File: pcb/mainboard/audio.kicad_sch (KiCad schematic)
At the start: 28 parts, among them J400 AudioJack3_SwitchT, U400 CS43130, U401 ADP150-1.8, U402 ADP150-1.8, Y400 22.5792MHz

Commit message: Mainboard schematics WIP
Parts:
- removed C400: 10uF, Capacitor_SMD:C_0402_1005Metric, symbol Device:C
- removed C416: 2.2uF, Capacitor_SMD:C_0402_1005Metric, symbol Device:C
- removed C417, C418: 1uF, Capacitor_SMD:C_0402_1005Metric, symbol Device:C
- removed J400: AudioJack3_SwitchT, footprint:PJ-327E, symbol symbols:AudioJack3_SwitchT
- removed R400: 33, Resistor_SMD:R_0402_1005Metric, symbol Device:R
- removed U400: CS43130, Package_DFN_QFN:QFN-40-1EP_5x5mm_P0.4mm_EP3.6x3.6mm_ThermalVias, symbol symbols:CS43130
- removed U401, U402: ADP150-1.8, footprint:CSP-4_2x2_0.8x0.8mm, symbol symbols:ADP150-1.8
- removed Y400: 22.5792MHz, Oscillator:Oscillator_SMD_Abracon_ASE-4Pin_3.2x2.5mm, symbol Device:Crystal_GND24
- added J401: AudioJack3, footprint:PJ-208, symbol Connector:AudioJack3
- added L401, L402: 120R, Inductor_SMD:L_0603_1608Metric, symbol Device:L
- added L403, L404: 15uH, Inductor_SMD:L_0603_1608Metric, symbol Device:L
- added LS401: Speaker, Buzzer_Beeper:Buzzer_D14mm_H7mm_P10mm, symbol Device:Speaker
- added R403, R404, R405: 22R, Resistor_SMD:R_0402_1005Metric, symbol Device:R
- added U402: FSA2269UMX, Package_DFN_QFN:UQFN-10_1.4x1.8mm_P0.4mm, symbol symbols:FSA2269UMX
- added U403: WM8978, Package_DFN_QFN:QFN-32-1EP_5x5mm_P0.5mm_EP3.45x3.45mm_ThermalVias, symbol symbols:WM8978
- C401, C402: value 100nF -> 220nF; LCSC (none) -> C880414; Ref.Price (none) -> 0.0036
- C403, C404: value 18pF -> 220nF; LCSC (none) -> C880414; Ref.Price (none) -> 0.0036
- C405: value 100nF -> 10uF/6.3V; footprint Capacitor_SMD:C_0402_1005Metric -> Capacitor_SMD:C_0603_1608Metric; LCSC (none) -> C105490; Ref.Price (none) -> 0.0165
- C406: value 4.7uF -> 10uF/6.3V; footprint Capacitor_SMD:C_0402_1005Metric -> Capacitor_SMD:C_0603_1608Metric; LCSC (none) -> C105490; Ref.Price (none) -> 0.0165
- C407, C408: value 2.2uF -> 1uF; LCSC (none) -> C157353; Ref.Price (none) -> 0.0034
- C409: value 15uF -> 220nF; footprint Capacitor_SMD:C_0603_1608Metric -> Capacitor_SMD:C_0402_1005Metric; LCSC (none) -> C880414; Ref.Price (none) -> 0.0036
- C410: value 15uF -> 100nF; footprint Capacitor_SMD:C_0603_1608Metric -> Capacitor_SMD:C_0402_1005Metric; LCSC (none) -> C56392; Ref.Price (none) -> 0.0023
- C411, C412: value 2.2uF -> 100uF; footprint Capacitor_SMD:C_0402_1005Metric -> Capacitor_SMD:C_1206_3216Metric; LCSC (none) -> C178304; Ref.Price (none) -> 0.1211
- C413, C414: value 2.2uF -> 100nF; LCSC (none) -> C56392; Ref.Price (none) -> 0.0023
- C415: value 2.2uF -> 220nF; LCSC (none) -> C880414; Ref.Price (none) -> 0.0036
- R401, R402: value 33 -> 22R; LCSC (none) -> C93929; Ref.Price (none) -> 0.002
- gave numbers to parts that had none: 1
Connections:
- net +3V3: now also L401.2, L402.2
- net GND: now also C409.2, C410.2, C413.1, C414.1, J401.S, U402.4 (GND), U403.12 (DGND), U403.18 (MODE), U403.24 (SPKGND), U403.28 (AGND), U403.33 (GND_PADDLE); no longer C401.2, C402.2, C403.2, C404.2, C407.2, C408.2, C414.2, C415.2
- net at C408.1: now also U403.6 (R2); no longer C409.1
- net at C403.1: now also C404.1, C406.1, L401.1, U403.26 (SPKVDD), U403.31 (AVDD)
- net at C411.1: now also U403.30 (HP_L)
- net at C413.2: now also C415.2, L404.2, LS401.2
- net at C415.1: now also C414.2, L403.2, LS401.1
- net at C412.1: now also U403.29 (HP_R); no longer C413.1
- net SAI_TX_BCLK: now reaches R402.1
- net SAI_TX_BCLK: now also U201.AD22 (SAI2_TXC)
- net SAI_TX_SYNC: now reaches R401.1
- net SAI_TX_SYNC: now also U201.AD23 (SAI2_TXFS)
- net at C407.1: now also U403.3 (L2); no longer C410.1
- net TASKSEL: now reaches U201.AB22 (SAI2_RXC)
- net TASKSEL: now also U402.6, U402.7
- net SAI_RX_DATA0: now reaches U201.AC24 (SAI2_RXD0)
- net SAI_RX_DATA0: now also R403.1
- net SAI_MCLK: now reaches U201.AD19 (SAI2_MCLK)
- net SAI_MCLK: now also R405.1
- net +1V8A renamed +1V8
- net +1V8: now also C409.1, U402.9 (VCC), U403.13 (DCVDD), U403.14 (DBVDD)
- net +3.3VA: no longer names the net of C405.1
- net +3.3VA: now also L402.1; no longer C406.1
- net SAI1_TX_BCLK: no longer names the net of R402.2
- net SAI1_TX_BCLK: now also U403.8 (BCLK); no longer U201.AD22 (SAI2_TXC)
- net SAI1_TX_DATA0 renamed SAI_TX_DATA0
- net SAI_TX_DATA0: now also R404.1
- net SAI1_TX_SYNC: no longer names the net of R401.2
- net SAI1_TX_SYNC: now also U403.7 (LRC); no longer U201.AD23 (SAI2_TXFS)
- new net: L403.1, U403.23 (SPK_P)
- new net: C401.2, C402.2, C403.2, C404.2
- new net: R403.2, U403.9 (ADCDAT)
- new net: R404.2, U403.10 (DACDAT)
- new net: R405.2, U403.11 (MCLK)
- new net: L404.1, U403.25 (SPK_N)
- new net: C410.1, U403.27 (VMID)
- new net: J401.R, U402.5
- new net: J401.T, U402.8
- new net HP_L: U402.10
- new net HP_R: U402.2
- new net I2C3_SCL: U403.16 (SCLK)
- new net I2C3_SDA: U403.17 (SDIN)
- new net LINEIN_L: C407.2, U402.1
- new net LINEIN_R: C408.2, U402.3
- no-connect marks 5 -> 40

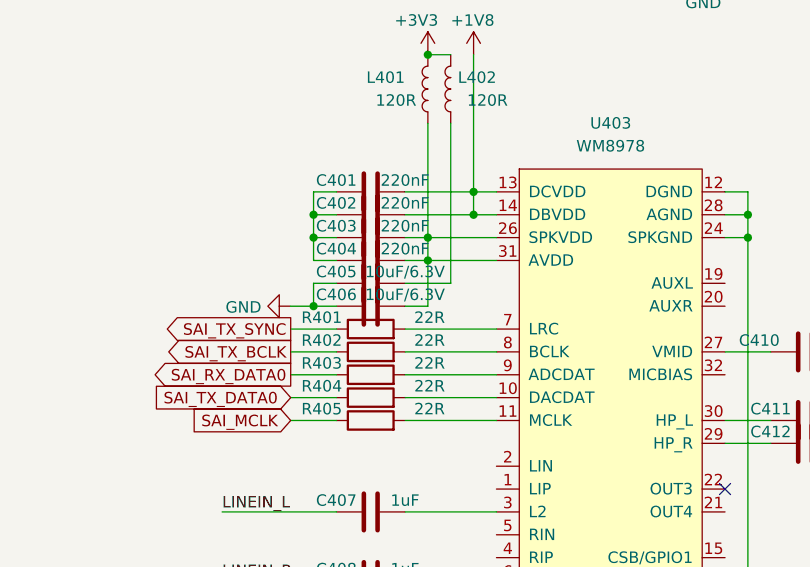
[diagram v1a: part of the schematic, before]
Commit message: Draft motherboard schematics for r0.0 layout
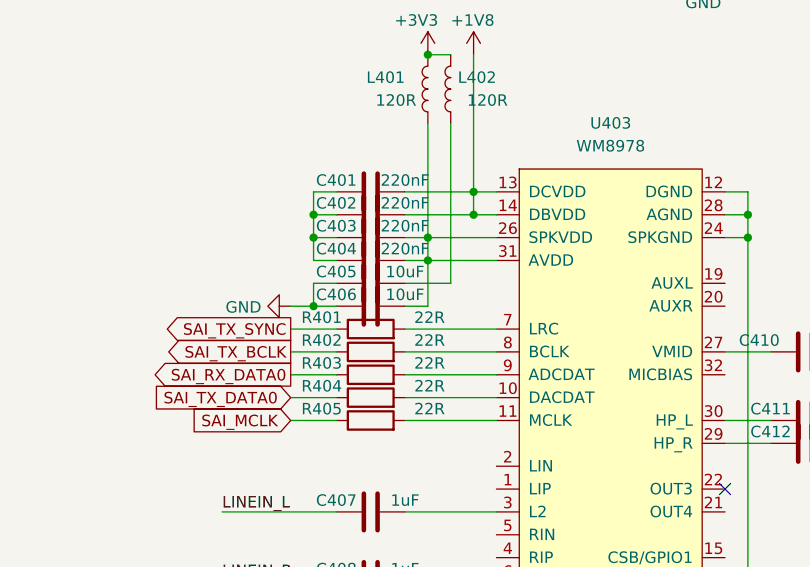
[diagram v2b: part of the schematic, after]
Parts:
- C401, C402, C403, C404, C409, C410, C413, C414, C415: footprint Capacitor_SMD:C_0402_1005Metric -> Capacitor_SMD:C_0201_0603Metric
- C405, C406: value 10uF/6.3V -> 10uF; footprint Capacitor_SMD:C_0603_1608Metric -> Capacitor_SMD:C_0402_1005Metric
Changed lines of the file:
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@@
     (property "Reference" "C409" (id 0) (at 218.44 67.31 0))
     (property "Value" "220nF" (id 1) (at 218.44 69.85 0))
-    (property "Footprint" "Capacitor_SMD:C_0402_1005Metric" (id 2) (at 214.3252 71.12 0)
+    (property "Footprint" "Capacitor_SMD:C_0201_0603Metric" (id 2) (at 214.3252 71.12 0)
       (effects (font (size 1.27 1.27)) hide)
     )
@@
     (in_bom yes) (on_board yes)
     (property "Reference" "C405" (id 0) (at 172.72 105.41 90))
-    (property "Value" "10uF/6.3V" (id 1) (at 180.34 105.41 90))
-    (property "Footprint" "Capacitor_SMD:C_0603_1608Metric" (id 2) (at 172.72 107.6452 0)
+    (property "Value" "10uF" (id 1) (at 180.34 105.41 90))
+    (property "Footprint" "Capacitor_SMD:C_0402_1005Metric" (id 2) (at 172.72 107.6452 0)
       (effects (font (size 1.27 1.27)) hide)
     )
@@
     (property "Reference" "C414" (id 0) (at 241.935 148.59 0))
     (property "Value" "100nF" (id 1) (at 242.57 153.67 0))
-    (property "Footprint" "Capacitor_SMD:C_0402_1005Metric" (id 2) (at 237.7948 147.32 0)
+    (property "Footprint" "Capacitor_SMD:C_0201_0603Metric" (id 2) (at 237.7948 147.32 0)
       (effects (font (size 1.27 1.27)) hide)
     )
@@
     (property "Reference" "C401" (id 0) (at 172.72 95.25 90))
     (property "Value" "220nF" (id 1) (at 180.34 95.25 90))
-    (property "Footprint" "Capacitor_SMD:C_0402_1005Metric" (id 2) (at 172.72 97.4852 0)
+    (property "Footprint" "Capacitor_SMD:C_0201_0603Metric" (id 2) (at 172.72 97.4852 0)
       (effects (font (size 1.27 1.27)) hide)
     )
@@
     (property "Reference" "C404" (id 0) (at 172.72 102.87 90))
     (property "Value" "220nF" (id 1) (at 180.34 102.87 90))
-    (property "Footprint" "Capacitor_SMD:C_0402_1005Metric" (id 2) (at 172.72 105.1052 0)
+    (property "Footprint" "Capacitor_SMD:C_0201_0603Metric" (id 2) (at 172.72 105.1052 0)
       (effects (font (size 1.27 1.27)) hide)
     )
@@
     (in_bom yes) (on_board yes)
     (property "Reference" "C406" (id 0) (at 172.72 107.95 90))
-    (property "Value" "10uF/6.3V" (id 1) (at 180.34 107.95 90))
-    (property "Footprint" "Capacitor_SMD:C_0603_1608Metric" (id 2) (at 172.72 110.1852 0)
+    (property "Value" "10uF" (id 1) (at 180.34 107.95 90))
+    (property "Footprint" "Capacitor_SMD:C_0402_1005Metric" (id 2) (at 172.72 110.1852 0)
       (effects (font (size 1.27 1.27)) hide)
     )
@@
     (property "Reference" "C413" (id 0) (at 234.315 148.59 0))
     (property "Value" "100nF" (id 1) (at 234.95 153.67 0))
-    (property "Footprint" "Capacitor_SMD:C_0402_1005Metric" (id 2) (at 230.1748 147.32 0)
+    (property "Footprint" "Capacitor_SMD:C_0201_0603Metric" (id 2) (at 230.1748 147.32 0)
       (effects (font (size 1.27 1.27)) hide)
     )
@@
     (property "Reference" "C415" (id 0) (at 240.03 138.43 90))
     (property "Value" "220nF" (id 1) (at 248.92 138.43 90))
-    (property "Footprint" "Capacitor_SMD:C_0402_1005Metric" (id 2) (at 248.92 138.7348 0)
+    (property "Footprint" "Capacitor_SMD:C_0201_0603Metric" (id 2) (at 248.92 138.7348 0)
       (effects (font (size 1.27 1.27)) hide)
     )
@@
     (property "Reference" "C410" (id 0) (at 219.71 113.03 90))
     (property "Value" "100nF" (id 1) (at 231.14 113.03 90))
-    (property "Footprint" "Capacitor_SMD:C_0402_1005Metric" (id 2) (at 228.6 113.3348 0)
+    (property "Footprint" "Capacitor_SMD:C_0201_0603Metric" (id 2) (at 228.6 113.3348 0)
       (effects (font (size 1.27 1.27)) hide)
     )
@@
     (property "Reference" "C402" (id 0) (at 172.72 97.79 90))
     (property "Value" "220nF" (id 1) (at 180.34 97.79 90))
-    (property "Footprint" "Capacitor_SMD:C_0402_1005Metric" (id 2) (at 172.72 100.0252 0)
+    (property "Footprint" "Capacitor_SMD:C_0201_0603Metric" (id 2) (at 172.72 100.0252 0)
       (effects (font (size 1.27 1.27)) hide)
     )
@@
     (property "Reference" "C403" (id 0) (at 172.72 100.33 90))
     (property "Value" "220nF" (id 1) (at 180.34 100.33 90))
-    (property "Footprint" "Capacitor_SMD:C_0402_1005Metric" (id 2) (at 172.72 102.5652 0)
-      (effects (font (size 1.27 1.27)) hide)
-    )
+    (property "Footprint" "Capacitor_SMD:C_0201_0603Metric" (id 2) (at 172.72 102.5652 0)
+      (effects (font (size 1.27 1.27)) hide)
+    )

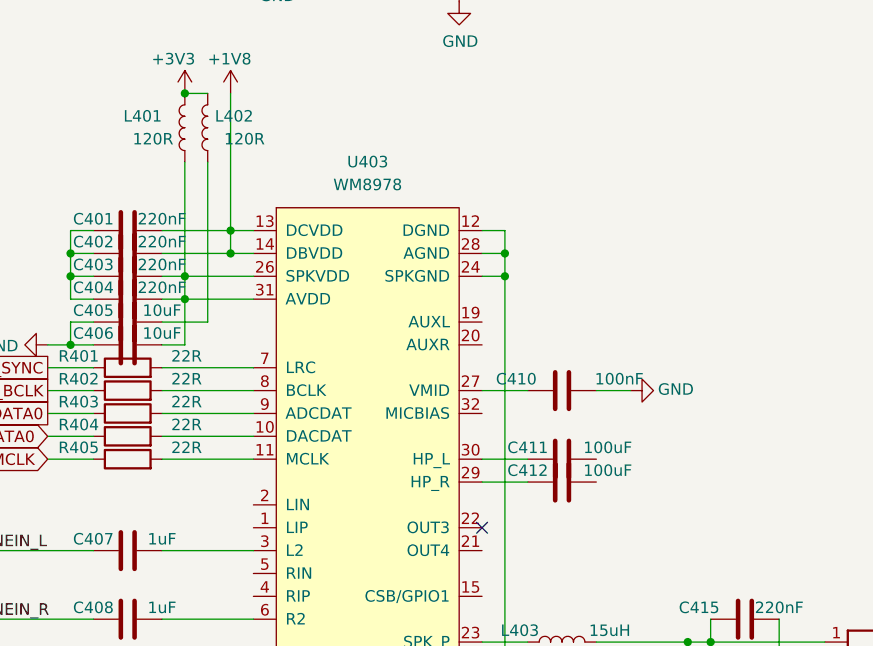
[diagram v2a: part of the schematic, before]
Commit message: Motherboard PCB component initial placement, schematics fixes
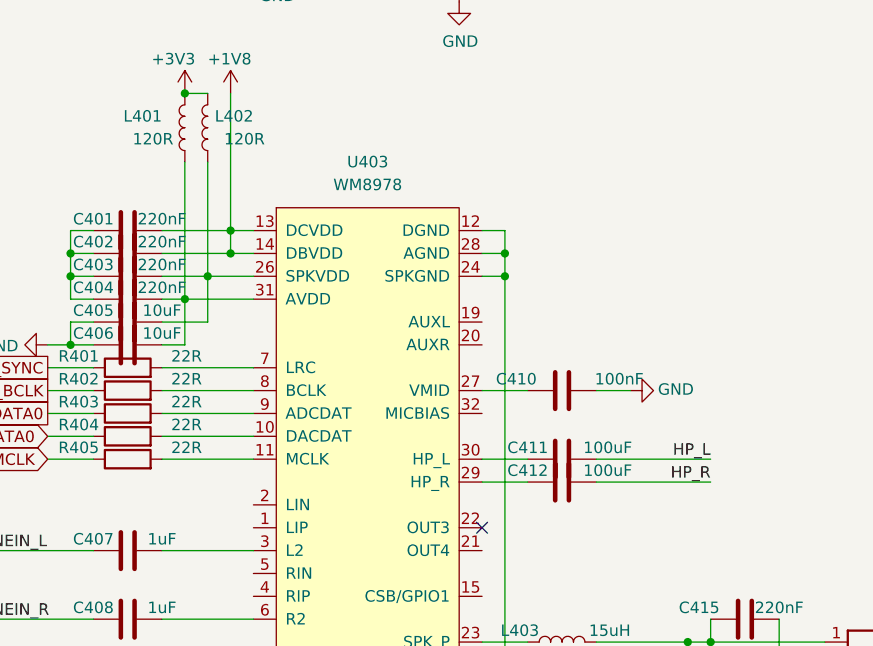
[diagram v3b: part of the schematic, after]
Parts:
- LS401: footprint Buzzer_Beeper:Buzzer_D14mm_H7mm_P10mm -> Buzzer_Beeper:Speaker_CUI_CMR-1206S-67
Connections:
- net HP_L: now also C411.2
- net HP_R: now also C412.2
- net at C405.1, L402.1: now also C403.1, U403.26 (SPKVDD)
- net at C404.1, C406.1, L401.1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: no longer C403.1, U403.26 (SPKVDD)
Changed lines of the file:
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@@
   (junction (at 182.88 81.28) (diameter 0.9144) (color 0 0 0 0)
   )
+  (junction (at 185.42 101.6) (diameter 0) (color 0 0 0 0)
+  )
   (junction (at 218.44 99.06) (diameter 0.9144) (color 0 0 0 0)
   )
@@
   )
   (junction (at 241.3 142.24) (diameter 0.9144) (color 0 0 0 0)
-  )
-  (junction (at 182.88 101.6) (diameter 0.9144) (color 0 0 0 0)
   )
   (junction (at 187.96 99.06) (diameter 0) (color 0 0 0 0)
@@
     (stroke (width 0) (type default) (color 0 0 0 0))
   )
-  (wire (pts (xy 182.88 101.6) (xy 180.34 101.6))
+  (wire (pts (xy 180.34 101.6) (xy 185.42 101.6))
     (stroke (width 0) (type solid) (color 0 0 0 0))
   )
@@
     (stroke (width 0) (type solid) (color 0 0 0 0))
   )
+  (wire (pts (xy 185.42 101.6) (xy 185.42 106.68))
+    (stroke (width 0) (type solid) (color 0 0 0 0))
+  )
   (wire (pts (xy 170.18 101.6) (xy 170.18 104.14))
     (stroke (width 0) (type solid) (color 0 0 0 0))
@@
     (stroke (width 0) (type solid) (color 0 0 0 0))
   )
-  (wire (pts (xy 185.42 88.9) (xy 185.42 106.68))
+  (wire (pts (xy 185.42 88.9) (xy 185.42 101.6))
     (stroke (width 0) (type solid) (color 0 0 0 0))
   )
@@
     (stroke (width 0) (type default) (color 0 0 0 0))
   )
-  (wire (pts (xy 182.88 101.6) (xy 190.5 101.6))
-    (stroke (width 0) (type solid) (color 0 0 0 0))
+  (wire (pts (xy 228.6 124.46) (xy 241.3 124.46))
+    (stroke (width 0) (type default) (color 0 0 0 0))
   )
   (wire (pts (xy 180.34 121.92) (xy 190.5 121.92))
@@
     (stroke (width 0) (type solid) (color 0 0 0 0))
   )
-  (wire (pts (xy 182.88 101.6) (xy 182.88 104.14))
+  (wire (pts (xy 228.6 121.92) (xy 241.3 121.92))
+    (stroke (width 0) (type default) (color 0 0 0 0))
+  )
+  (wire (pts (xy 182.88 88.9) (xy 182.88 104.14))
     (stroke (width 0) (type solid) (color 0 0 0 0))
   )
@@
     (stroke (width 0) (type default) (color 0 0 0 0))
   )
-  (wire (pts (xy 182.88 88.9) (xy 182.88 101.6))
-    (stroke (width 0) (type solid) (color 0 0 0 0))
-  )
   (wire (pts (xy 226.06 48.26) (xy 228.6 48.26))
     (stroke (width 0) (type default) (color 0 0 0 0))
@@
   (wire (pts (xy 187.96 144.78) (xy 190.5 144.78))
     (stroke (width 0) (type default) (color 0 0 0 0))
+  )
+  (wire (pts (xy 185.42 101.6) (xy 190.5 101.6))
+    (stroke (width 0) (type solid) (color 0 0 0 0))
   )
   (wire (pts (xy 195.58 40.64) (xy 182.88 40.64))
@@
     (effects (font (size 1.27 1.27)) (justify left bottom))
   )
+  (label "HP_R" (at 241.3 124.46 180)
+    (effects (font (size 1.27 1.27)) (justify right bottom))
+  )
   (label "HP_R" (at 182.88 50.8 0)
     (effects (font (size 1.27 1.27)) (justify left bottom))
@@
   (label "LINEIN_L" (at 160.02 132.08 0)
     (effects (font (size 1.27 1.27)) (justify left bottom))
+  )
+  (label "HP_L" (at 241.3 121.92 180)
+    (effects (font (size 1.27 1.27)) (justify right bottom))
   )
   (global_label "SAI_TX_DATA0" (shape output) (at 90.17 137.16 0)
@@
       (effects (font (size 1.27 1.27)) (justify left))
     )
-    (property "Footprint" "Buzzer_Beeper:Buzzer_D14mm_H7mm_P10mm" (id 2) (at 259.08 147.32 0)
-      (effects (font (size 1.27 1.27)) hide)
-    )
+    (property "Footprint" "Buzzer_Beeper:Speaker_CUI_CMR-1206S-67" (id 2) (at 259.08 147.32 0)
+      (effects (font (size 1.27 1.27)) hide)
+    )
